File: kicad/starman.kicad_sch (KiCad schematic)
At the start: 225 parts, among them J1 M20-8771246, J10 Barrel_Jack_MountingPin, J11 Conn_02x01, J2 M20-8771246, J3 M20-8771246, J4 ESW-106-44-T-S, J6 ESW-112-44-T-S, J7 Conn_01x10, J8 ESW-112-44-T-S, J9 Conn_01x10, SW1 SW_SPST, SW2 SW_SPST, U1 ESP32-S2-MINI-1, U10 LED1642GWTTR, U11 NCP59301, U12 LF33, U3 LED1642GWTTR, U4 LED1642GWTTR, U5 LED1642GWTTR, U6 LED1642GWTTR, U7 LED1642GWTTR, U8 LED1642GWTTR, U9 LED1642GWTTR, X2 ECS-2333-300, X3 ECS-2333-300

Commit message: Additional routing around new LED chips, cleaned up DRC errors and warnings
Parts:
- removed C28, C29: (no value), Capacitor_SMD:C_0805_2012Metric, symbol Device:C
- removed R14, R20: 500k, Resistor_SMD:R_0805_2012Metric, symbol Device:R
- added C17, C18: 1uF, Capacitor_SMD:C_0805_2012Metric, symbol Device:C
- added R17, R18: 500k, Resistor_SMD:R_0805_2012Metric, symbol Device:R
- C19: renamed from C30; value (none) -> 1uF
- C20: renamed from C19; value (none) -> 47uF
- C21: renamed from C20; value (none) -> 47uF
- C22: renamed from C21; value (none) -> 47uF
- C23: renamed from C22; value (none) -> 47uF
- C24: renamed from C23; value (none) -> 47uF
- C25: renamed from C24; value (none) -> 47uF
- C26: renamed from C25; value (none) -> 47uF
- C27: renamed from C26; value (none) -> 47uF
- C28: renamed from C27; value (none) -> 47uF
- C8: value (none) -> 1uF
- J5: value (none) -> Conn_02x03; footprint (none) -> Connector_PinHeader_2.54mm:PinHeader_2x03_P2.54mm_Vertical
- R10, R11, R12, R13, R8, R9: value (none) -> 11k
- R14: renamed from R16; value (none) -> 11k
- R15: renamed from R17; value (none) -> 11k
- R16: renamed from R18; value (none) -> 11k
- R19: value (none) -> 500k
- R20: renamed from R15; value (none) -> 500k
- U2: value (none) -> LED1642GWTTR; footprint (none) -> Package_SO:TSSOP-24_4.4x7.8mm_P0.65mm
- X1: value (none) -> ECS-2333-300; footprint (none) -> Oscillator:Oscillator_SMD_ECS_2520MV-xxx-xx-4Pin_2.5x2.0mm
- renumbered C16 to C14, C17 to C15, C18 to C16, C14 to C29, C15 to C30
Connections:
- net +3V3: now also C19.2, X1.4 (VDD), X2.4 (VDD), C17.2, C18.2, R17.1, R18.1
- net GND: now also C17.1, C18.1
- net PWCLK1: now also R17.2
- net PWCLK2: now also R18.2
- net PWCLK3: no longer C19.2
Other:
- moved on the sheet: C19, R19, X3

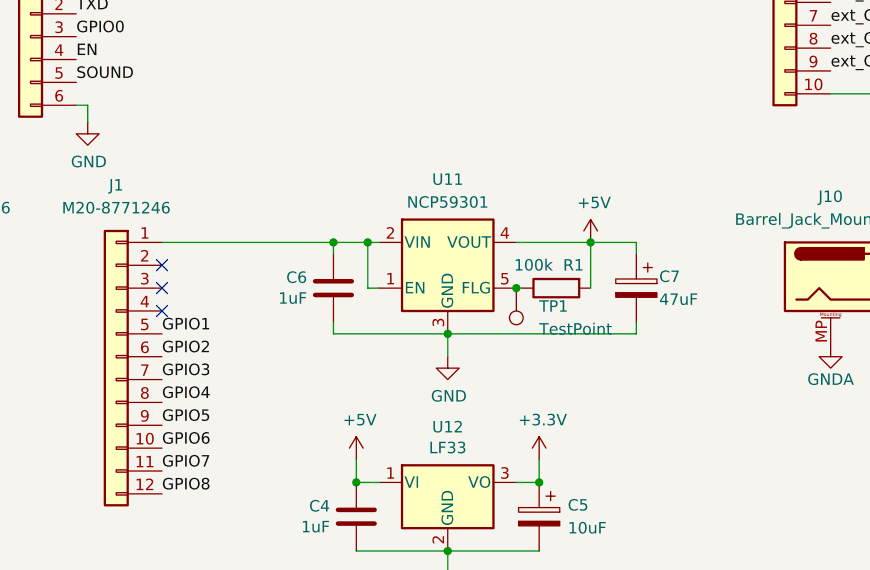
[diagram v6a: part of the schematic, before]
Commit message: Move from NCP59301 to AP1084
Cheaper and provides 5V 5A
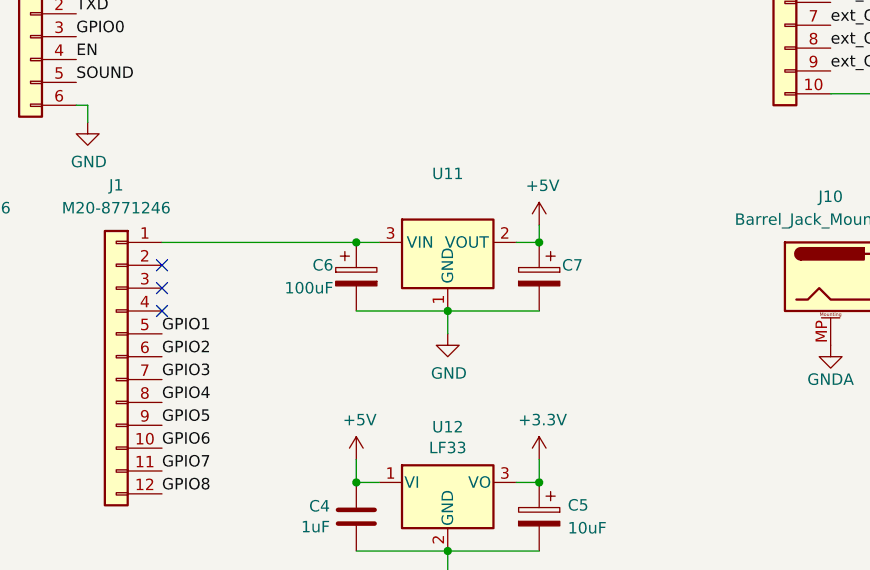
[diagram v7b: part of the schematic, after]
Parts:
- removed C6: 1uF, Capacitor_SMD:C_0805_2012Metric, symbol Device:C
- removed R1: 100k, Resistor_SMD:R_0805_2012Metric, symbol Device:R
- removed TP1: TestPoint, TestPoint:TestPoint_Pad_1.5x1.5mm, symbol Connector:TestPoint
- removed U11: NCP59301, Package_TO_SOT_SMD:TO-263-5_TabPin3, symbol starman:NCP59300
- added C6: 100uF, Capacitor_Tantalum_SMD:CP_EIA-3216-10_Kemet-I, symbol starman-rescue:CP-Device
- added U11: (no value), symbol starman:AP1084
- C7: value 47uF -> (none)
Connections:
- net +5V: now also U11.2 (VOUT)
- net GND: now also C6.2, U11.1 (GND)
- net at J1.1 (Pin_1): now also C6.1, U11.3 (VIN)
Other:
- moved on the sheet: C7

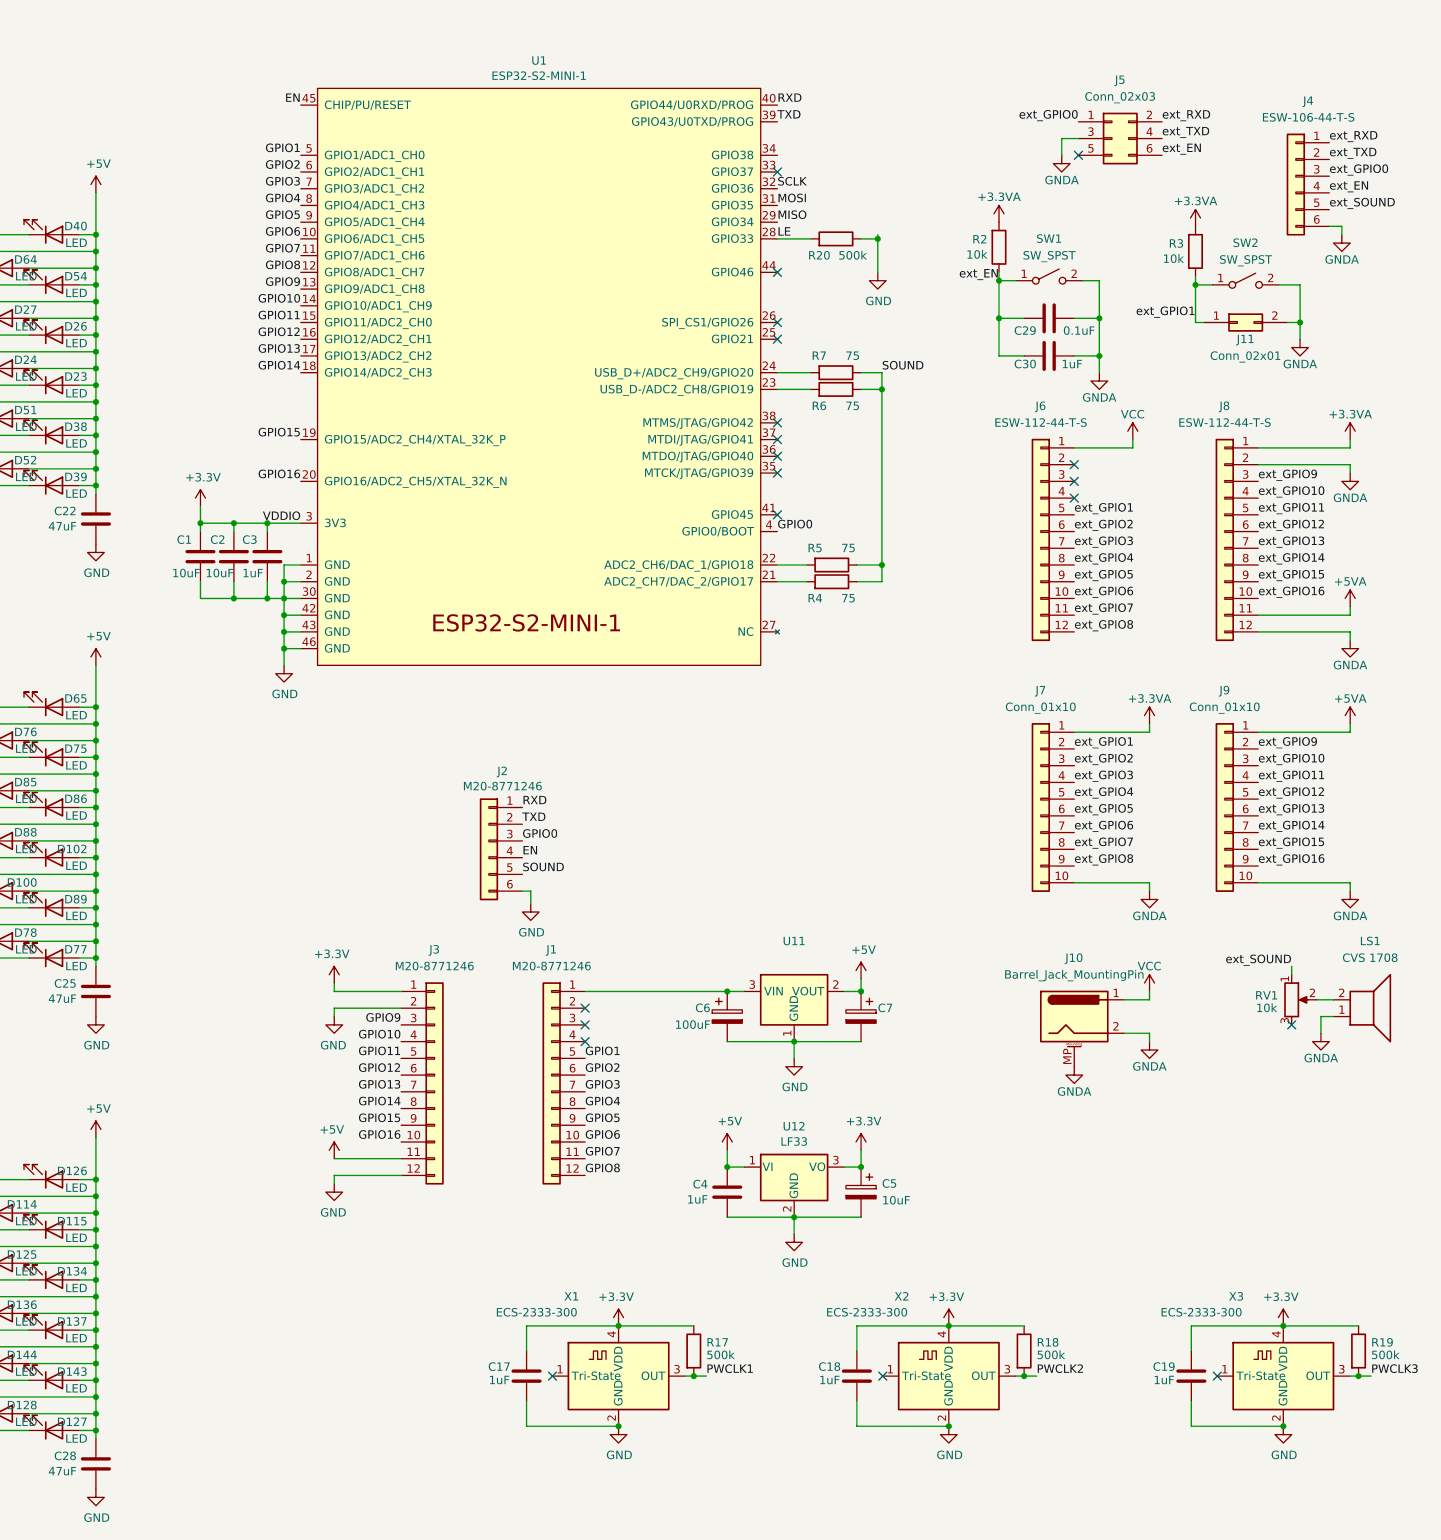
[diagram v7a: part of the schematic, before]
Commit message: Moved caps and rs from ext to onboard star to make room for potential opamp
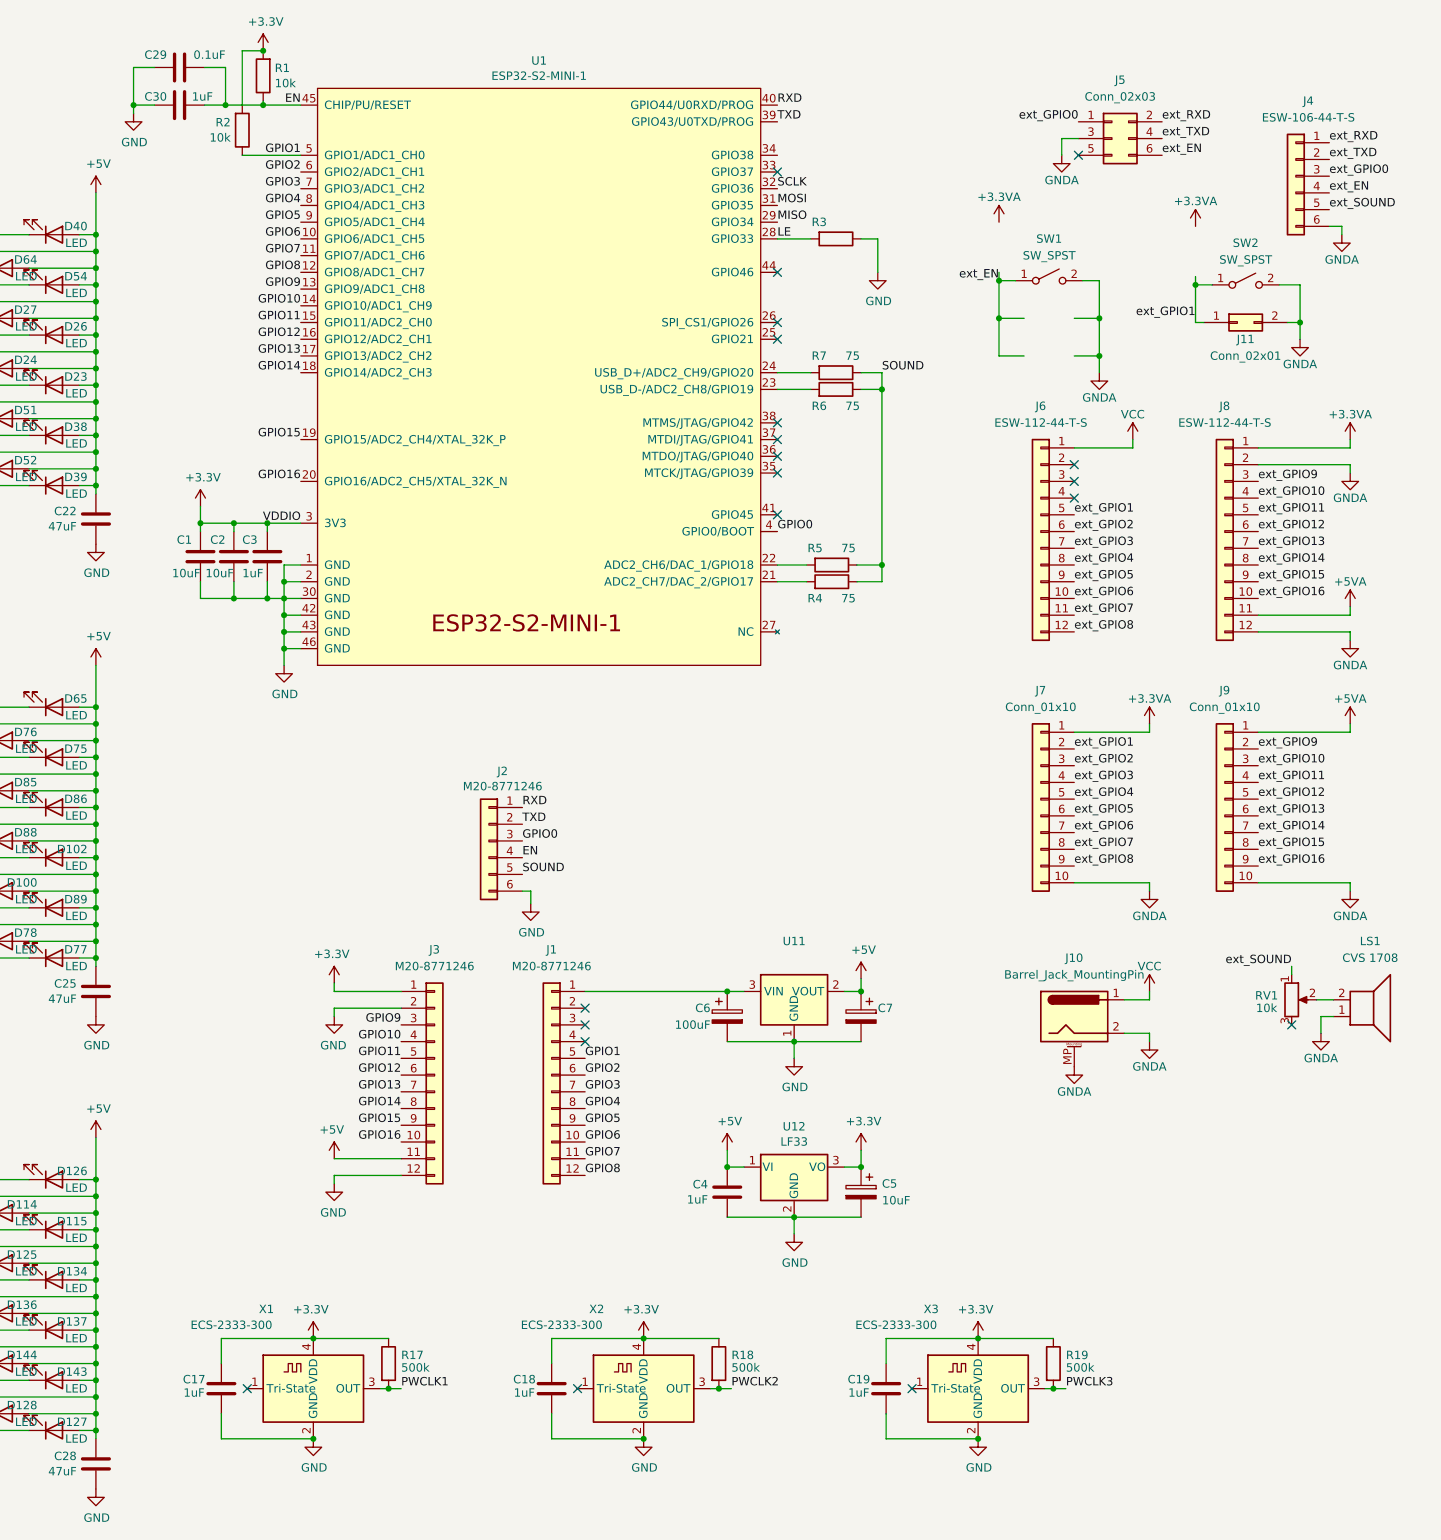
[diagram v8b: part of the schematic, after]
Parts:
- R3: renamed from R20; value 500k -> (none); footprint Resistor_SMD:R_0805_2012Metric -> (none)
- renumbered R2 to R1, R3 to R2
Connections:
- net +3.3VA: no longer R1.2, R2.2
- net +3V3: now also R1.2, R2.2
- net EN: now also C29.1, C30.1, R1.1
- net GND: now also C29.2, C30.2
- net GNDA: no longer C29.1, C30.1
- net GPIO1: now also R2.1
- net ext_EN: no longer C29.2, C30.2, R1.1
- net ext_GPIO1: no longer R2.1
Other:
- moved on the sheet: C17, C18, C19, C29, C30, R1, R17, R18, R19, R2, X1, X2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
